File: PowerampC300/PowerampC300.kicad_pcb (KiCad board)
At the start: 2 copper layers, 240 x 63 mm, 109 parts, among them J1 Conn_01x02, J2 Conn_01x02, J3 Conn_01x02, J4 Conn_01x01, J5 Conn_01x01, J6 Conn_01x01, J7 Conn_01x01, J8 Conn_01x02, J9 Conn_Coaxial, Q1 2N5551, Q10 MJE15033, Q11 MJE15032, Q12 MJE15032, Q13 2N5551, Q14 2N5401, Q15 MJE15032, Q16 MJE15033, Q17 MJL3281A, Q18 MJL1302A, Q19 MJL3281A, Q2 2N5551, Q20 MJL1302A, Q21 MJL3281A, Q22 MJL1302A, Q23 MJL3281A, Q24 MJL1302A, Q3 2N5401, Q4 2N5401, Q5 2N5551, Q6 2N5551, Q7 2N5551, Q8 2N5401, Q9 2N5401

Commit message: JLCPCB order 2020-09-21
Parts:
- moved C11 177.3 mm to (230.3, 92.4), turned to 90 degrees
- moved R41 155.0 mm to (226.8, 82.4), turned to 90 degrees
- moved C19 53.2 mm to (253.0, 94.2), turned to 90 degrees
- moved L1 51.6 mm to (209.6, 82.0), turned to 90 degrees
- moved C14 47.9 mm to (257.4, 78.8)
- moved J3 40.5 mm to (41.8, 90.5), turned to 180 degrees
- moved D9 37.7 mm to (57.6, 101.4), turned to 0 degrees
- moved D7 31.0 mm to (46.7, 101.5), turned to 0 degrees
- moved J2 26.8 mm to (242.0, 95.6), turned to 180 degrees
- moved J1 24.6 mm to (220.9, 100.9), turned to 180 degrees
- moved C18 22.4 mm to (242.0, 78.8), turned to 90 degrees
- moved D1 21.1 mm to (75.8, 93.0), turned to 0 degrees
- moved R13 20.7 mm to (71.2, 93.4)
- moved C8 20.7 mm to (79.6, 70.4)
- moved C7 20.5 mm to (79.8, 86.8)
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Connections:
- C11 pad 1: Net-(C11-Pad1) -> GND
- C6 pad 2: Net-(C11-Pad2) -> Net-(C6-Pad2)
- D5 pad 2: Net-(C11-Pad2) -> Net-(C6-Pad2)
- D6 pad 1: Net-(C11-Pad2) -> Net-(C6-Pad2)
- L1 pad 2: Net-(C11-Pad2) -> Net-(C6-Pad2)
- Q13 pad 1: Net-(C11-Pad2) -> Net-(C6-Pad2)
- Q14 pad 1: Net-(C11-Pad2) -> Net-(C6-Pad2)
- R14 pad 1: Net-(C11-Pad2) -> Net-(C6-Pad2)
- R26 pad 2: Net-(C11-Pad2) -> Net-(C6-Pad2)
- R27 pad 1: Net-(C11-Pad2) -> Net-(C6-Pad2)
- R31 pad 1: Net-(C11-Pad2) -> Net-(C6-Pad2)
- R32 pad 2: Net-(C11-Pad2) -> Net-(C6-Pad2)
- R33 pad 1: Net-(C11-Pad2) -> Net-(C6-Pad2)
- R34 pad 2: Net-(C11-Pad2) -> Net-(C6-Pad2)
- R35 pad 1: Net-(C11-Pad2) -> Net-(C6-Pad2)
- R36 pad 2: Net-(C11-Pad2) -> Net-(C6-Pad2)
- R37 pad 1: Net-(C11-Pad2) -> Net-(C6-Pad2)
- R38 pad 2: Net-(C11-Pad2) -> Net-(C6-Pad2)
- R39 pad 1: Net-(C11-Pad2) -> Net-(C6-Pad2)
- R40 pad 2: Net-(C11-Pad2) -> Net-(C6-Pad2)
- R41 pad 1: GND -> Net-(C11-Pad2)
- R41 pad 2: Net-(C11-Pad1) -> Net-(C6-Pad2)
- R42 pad 1: Net-(C11-Pad2) -> Net-(C6-Pad2)
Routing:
- net Net-(C6-Pad2): track 0.00 -> 454.9 mm, vias 0 -> 1
- net Net-(C11-Pad2): track 406.1 -> 3.54 mm
- net -48V: track 319.7 -> 298.7 mm
- net Net-(C4-Pad2): track 56.0 -> 44.0 mm
- net OUTPUT: track 40.7 -> 28.8 mm
- net Net-(D10-Pad2): track 3.78 -> 10.8 mm
- net Net-(C11-Pad1): track 6.99 -> 0.00 mm
- net +48V: track 301.1 -> 308.0 mm
- net Net-(R10-Pad2): track 52.0 -> 55.8 mm
- net Net-(Q10-Pad1): track 38.4 -> 41.9 mm
- net INPUT: track 25.2 -> 22.0 mm
- net Net-(C1-Pad1): track 10.2 -> 12.9 mm
- net Net-(C22-Pad1): track 39.6 -> 42.1 mm
- net Net-(R10-Pad3): track 15.8 -> 13.4 mm
- net Net-(C9-Pad1): track 28.9 -> 31.2 mm
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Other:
- board text added: "MODIFIED C300 AMPLIFIER BY DANIEL MARKS ORIGINAL BY MICHAEL CHUA (AMPSLAB) CC-BY-SA 4.0 V2"
- board text removed: "C300 AMPLIFIER PCB BY DANIEL MARKS C300 DESIGNED BY MICHAEL CHUA (AMPSLAB) CC-BY-SA 4.0 V2"

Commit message: Working design 2020-10-12
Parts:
- removed Q9: 2N5401, TO_SOT_Packages_THT:TO-92_Inline_Wide
- removed R18: 330R, Resistors_THT:R_Axial_DIN0207_L6.3mm_D2.5mm_P7.62mm_Horizontal
- removed R20: 27R, Resistors_THT:R_Axial_DIN0207_L6.3mm_D2.5mm_P7.62mm_Horizontal
- added R43: 10k, Resistors_THT:R_Axial_DIN0309_L9.0mm_D3.2mm_P12.70mm_Horizontal, F.Cu at (193.8, 101.5)
- C3: value 220 pF -> 150 pF
- C9: value 100 pF -> 150 pF
- R19: value 10R -> 33R; footprint Resistors_THT:R_Axial_DIN0207_L6.3mm_D2.5mm_P7.62mm_Horizontal -> Resistors_THT:R_Axial_DIN0309_L9.0mm_D3.2mm_P12.70mm_Horizontal
- R23: value 150R -> 100R
- R5: value 620R -> 1k
- moved R19 7.10 mm to (111.1, 81.8)
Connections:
- R19 pad 1: Net-(Q9-Pad2) -> Net-(Q10-Pad3)
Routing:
- net Net-(C6-Pad2): track 454.9 -> 479.1 mm
- net Net-(Q9-Pad2): track 15.6 -> 0.00 mm
- net +48V: track 308.0 -> 301.7 mm
- net Net-(Q9-Pad1): track 5.95 -> 0.00 mm
- net Net-(Q10-Pad3): track 11.0 -> 13.2 mm
- net Net-(Q10-Pad1): track 41.9 -> 39.8 mm

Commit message: Changed grounding and star layout
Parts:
- removed C20, C21: 0.1 uF, Capacitors_THT:C_Disc_D5.0mm_W2.5mm_P5.00mm
- added C24: 0.1 uF, Capacitors_THT:C_Axial_L3.8mm_D2.6mm_P10.00mm_Horizontal, F.Cu at (121.6, 92.8)
- added C25: SHORT, Capacitors_THT:C_Disc_D5.0mm_W2.5mm_P5.00mm, F.Cu at (134.9, 93.0)
- added JP1: Jumper_NO_Small, Pin_Headers:Pin_Header_Straight_1x02_Pitch2.54mm, F.Cu at (263.5, 93.5)
- added JP2: Jumper_NO_Small, Pin_Headers:Pin_Header_Straight_1x02_Pitch2.54mm, F.Cu at (28.8, 94.1)
- added R18: NC, Resistors_THT:R_Axial_DIN0207_L6.3mm_D2.5mm_P7.62mm_Horizontal, F.Cu at (111.5, 90.6)
- moved C8 24.8 mm to (77.0, 95.1), turned to 90 degrees
- moved D10 21.9 mm to (248.0, 103.0)
- moved D8 16.6 mm to (248.0, 100.0)
- moved C7 8.17 mm to (77.0, 79.1), turned to 270 degrees
- moved C16 7.85 mm to (39.9, 80.2), turned to 90 degrees
- moved J2 7.60 mm to (242.0, 88.0)
- moved C12 7.46 mm to (54.6, 80.2), turned to 90 degrees
- moved C23 7.28 mm to (66.0, 104.3)
- moved C17 7.00 mm to (54.8, 95.0), turned to 90 degrees
- moved R13 6.83 mm to (64.9, 90.7)
- moved D1 6.80 mm to (70.0, 96.5), turned to 270 degrees
- moved R2 5.25 mm to (161.0, 94.0)
- moved R19 4.20 mm to (106.9, 81.5)
- moved C1 3.29 mm to (158.0, 90.0)
- moved C9 3.16 mm to (112.6, 93.8)
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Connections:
- C9 pad 2: Net-(C10-Pad2) -> Net-(C25-Pad1)
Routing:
- net Net-(C25-Pad1): track 0.00 -> 31.4 mm
- net Net-(C23-Pad2): track 26.3 -> 41.1 mm
- net Net-(C4-Pad2): track 44.0 -> 51.7 mm
- net +48V: track 301.7 -> 309.0 mm
- net INPUT: track 22.0 -> 27.3 mm
- net -48V: track 298.7 -> 304.0 mm
- net Net-(C3-Pad2): track 30.9 -> 35.7 mm
- net Net-(C10-Pad2): track 91.8 -> 87.8 mm
- net Net-(C9-Pad1): track 31.2 -> 27.4 mm
- net Net-(C24-Pad1): track 0.00 -> 3.41 mm
- net Net-(J4-Pad1): track 5.58 -> 8.50 mm
- net Net-(C6-Pad2): track 479.1 -> 476.4 mm
- net Net-(C1-Pad1): track 12.9 -> 15.6 mm
- net Net-(Q10-Pad1): track 39.8 -> 42.4 mm
- net Net-(Q10-Pad3): track 13.2 -> 15.4 mm
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
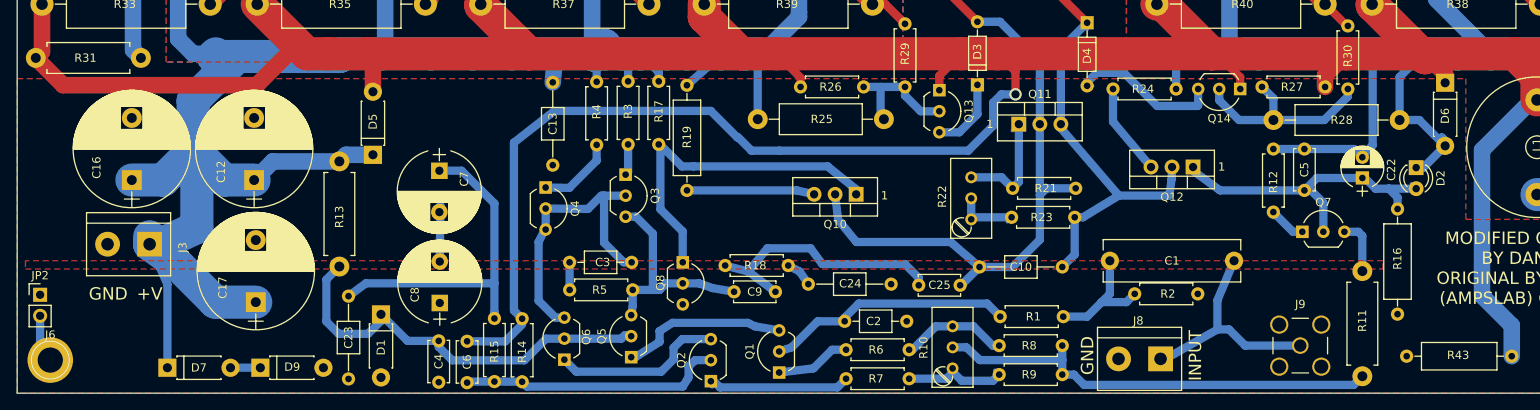
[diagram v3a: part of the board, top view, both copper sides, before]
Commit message: Sample feedback from output directly
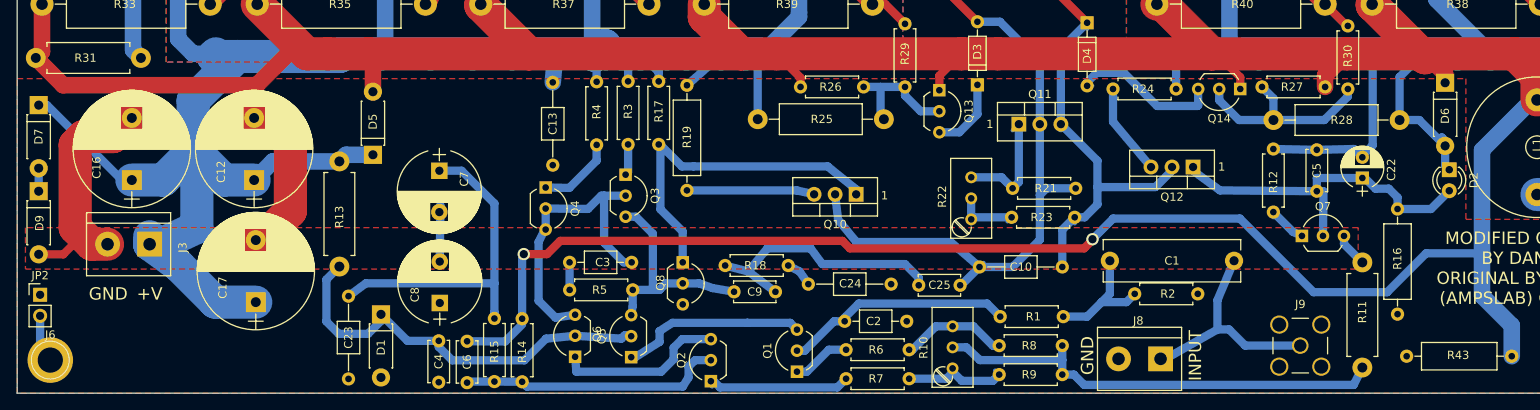
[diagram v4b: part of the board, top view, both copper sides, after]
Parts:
- moved D7 35.3 mm to (28.6, 71.2), turned to 270 degrees
- moved D9 34.2 mm to (28.6, 81.6), turned to 270 degrees
- moved D2 4.01 mm to (199.0, 79.0)
- moved Q1 2.15 mm to (120.2, 103.4)
- moved C5 1.50 mm to (183.0, 76.6)
- moved Q6 1.35 mm to (93.4, 101.6)
- moved R11 1.05 mm to (188.5, 90.2)
- moved Q7 0.50 mm to (181.2, 87.0)
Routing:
- net GND: track 0.75 -> 52.5 mm
- net Net-(C6-Pad2): track 476.4 -> 512.4 mm, vias 1 -> 2
- net -48V: track 304.0 -> 300.6 mm
- net Net-(C22-Pad1): track 41.5 -> 44.8 mm
- net Net-(Q7-Pad3): track 8.24 -> 5.07 mm
- net Net-(Q1-Pad3): track 20.9 -> 23.3 mm
- net Net-(C2-Pad2): track 31.2 -> 29.1 mm
- net Net-(Q1-Pad1): track 9.04 -> 7.03 mm
- net Net-(C3-Pad2): track 35.7 -> 37.0 mm
- net Net-(C10-Pad1): track 65.8 -> 64.6 mm
- net Net-(R10-Pad2): track 55.8 -> 56.6 mm
- net Net-(D7-Pad2): track 3.60 -> 2.78 mm

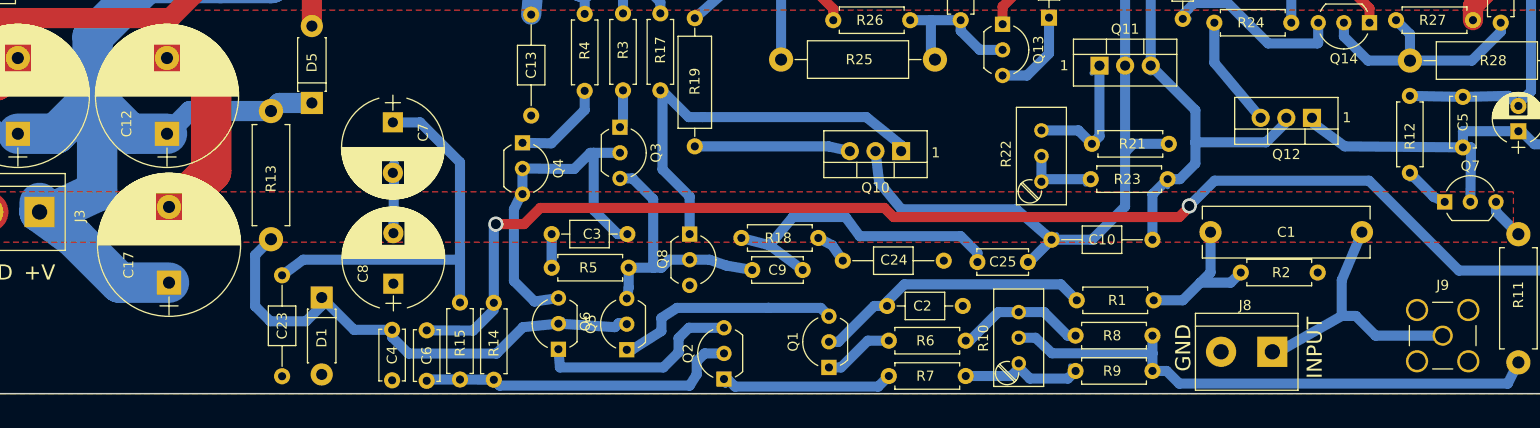
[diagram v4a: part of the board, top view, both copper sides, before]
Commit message: Moved Q1 and Q2 together
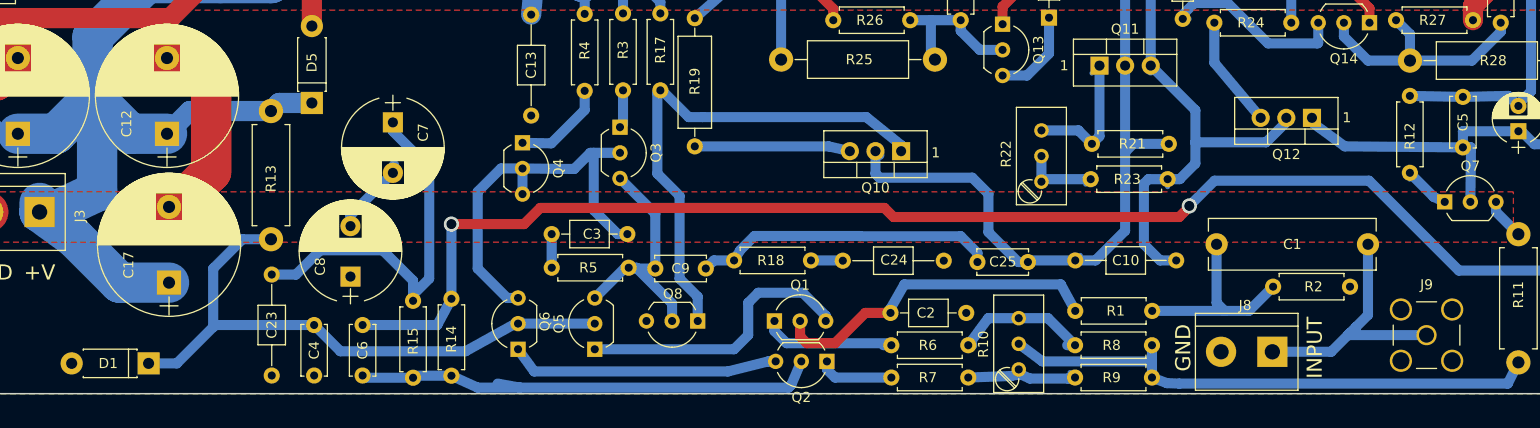
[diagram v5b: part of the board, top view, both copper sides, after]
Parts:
- moved D1 18.3 mm to (52.8, 103.0), turned to 180 degrees
- moved Q2 10.3 mm to (120.0, 102.8), turned to 180 degrees
- moved C9 9.60 mm to (103.0, 93.6)
- moved Q8 8.65 mm to (107.2, 98.8), turned to 180 degrees
- moved C4 7.74 mm to (69.2, 104.2)
- moved Q1 7.09 mm to (114.8, 98.8), turned to 0 degrees
- moved C6 6.37 mm to (74.0, 104.2)
- moved R15 4.65 mm to (79.0, 96.8)
- moved C8 4.31 mm to (72.8, 94.4)
- moved R14 4.22 mm to (82.8, 96.6)
- moved Q6 4.00 mm to (89.4, 101.6)
- moved R2 3.49 mm to (164.2, 95.4)
- moved Q5 3.18 mm to (97.0, 101.6)
- moved C10 3.12 mm to (154.6, 92.8)
- moved R18 2.34 mm to (110.8, 92.8)
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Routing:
- net Net-(C6-Pad1): track 33.2 -> 48.5 mm
- net Net-(Q2-Pad1): track 18.7 -> 7.99 mm
- net Net-(Q10-Pad1): track 42.4 -> 51.9 mm
- net Net-(C4-Pad2): track 51.8 -> 61.0 mm
- net Net-(C6-Pad2): track 512.4 -> 519.5 mm
- net Net-(Q1-Pad1): track 7.03 -> 13.9 mm
- net Net-(Q2-Pad3): track 20.5 -> 26.8 mm
- net Net-(Q1-Pad3): track 23.3 -> 29.3 mm
- net Net-(C2-Pad2): track 29.1 -> 35.0 mm
- net Net-(C10-Pad1): track 64.6 -> 70.4 mm
- net Net-(C1-Pad1): track 15.6 -> 19.9 mm
- net Net-(C3-Pad2): track 37.0 -> 41.2 mm
- net Net-(C10-Pad2): track 87.8 -> 91.5 mm
- net Net-(C23-Pad2): track 41.1 -> 38.1 mm
- net Net-(C9-Pad1): track 27.4 -> 25.4 mm
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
